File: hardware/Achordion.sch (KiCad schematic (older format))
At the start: 98 parts, among them J1 Power, J10 Jack, J11 Jack, J4 Jack, J5 Jack, J6 Jack, J7 Jack, J8 Jack, J9 Jack, SW2 Button, U4 LM4040C10, U6 TL072, U7 MCP6002, U8 MCP6002, U9 MCP6002

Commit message: Convert PCB to two stacked layers
This completely reworked layout should be much easier to solder and also
follows new front panel layout.

Signed-off-by: Petr Horacek <hrck@protonmail.com>
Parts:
- removed C39: 100n, Capacitor_SMD:C_0603_1608Metric_Pad1.08x0.95mm_HandSolder, symbol Device:C_Small
- removed C45, C47: 3n3, Capacitor_SMD:C_0603_1608Metric_Pad1.08x0.95mm_HandSolder, symbol Device:C_Small
- removed J11: Jack, Connector_Audio:Jack_3.5mm_QingPu_WQP-PJ398SM_Vertical_CircularHoles, symbol Connector:AudioJack2_SwitchT
- removed R15, R16, R49: 10k, Resistor_SMD:R_0603_1608Metric_Pad0.98x0.95mm_HandSolder, symbol Device:R_Small
- removed R32: 200k, Resistor_SMD:R_0603_1608Metric_Pad0.98x0.95mm_HandSolder, symbol Device:R_Small
- removed R33: 100k, Resistor_SMD:R_0603_1608Metric_Pad0.98x0.95mm_HandSolder, symbol Device:R_Small
- removed R34: 33k, Resistor_SMD:R_0603_1608Metric_Pad0.98x0.95mm_HandSolder, symbol Device:R_Small
- removed U7, U8: MCP6002, Package_SO:SOIC-8_3.9x4.9mm_P1.27mm, symbol Amplifier_Operational:MCP6002-xSN
- added J11: A I/O, Connector_PinHeader_2.54mm:PinHeader_2x06_P2.54mm_Vertical, symbol Connector_Generic:Conn_02x06_Odd_Even
- added J12: Debug, Connector_PinHeader_2.54mm:PinHeader_1x05_P2.54mm_Vertical, symbol Connector_Generic:Conn_01x05
- added J13: A IFACE, Connector_PinHeader_2.54mm:PinHeader_2x08_P2.54mm_Vertical, symbol Connector_Generic:Conn_02x08_Odd_Even
- added J2: B IFACE, Connector_PinSocket_2.54mm:PinSocket_2x08_P2.54mm_Vertical, symbol Connector_Generic:Conn_02x08_Odd_Even
- added J3: B I/O, Connector_PinSocket_2.54mm:PinSocket_2x06_P2.54mm_Vertical, symbol Connector_Generic:Conn_02x06_Odd_Even
- added U1: MCP6004, Package_SO:SOIC-14_3.9x8.7mm_P1.27mm, symbol Amplifier_Operational:MCP6004
- A1: value DaisySeed_Rev4 -> Daisy Seed v4; footprint Socket_DaisySeed:DaisySeed -> Device_Audio_Electrosmith_Daisy_Seed:Device_Audio_Electrosmith_Daisy_Seed
- C21: footprint Capacitor_SMD:C_1206_3216Metric_Pad1.33x1.80mm_HandSolder -> Capacitor_SMD:C_0603_1608Metric_Pad1.08x0.95mm_HandSolder
- D10, D3, D4, D5, D6, D7, D8, D9: value LED_Small -> LED
- FB1, FB2: value Ferrite_Bead_Small -> FB
- J1: footprint Connector_PinHeader_2.54mm:PinHeader_2x05_P2.54mm_Vertical -> Connector_IDC:IDC-Header_2x05_P2.54mm_Vertical
- RV1, RV2, RV3, RV4: footprint Potentiometer_THT:Potentiometer_Alps_RK09L_Single_Vertical -> Potentiometer_THT:Potentiometer_Alpha_RD901F-40-00D_Single_Vertical
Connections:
- net +3.3VA: now also J13.7 (Pin_7), J2.7 (Pin_7), U1.4 (V+)
- net CV1: now also A1.24 (ADC_INP5), C41.1, R22.2, U1.7; no longer A1.27 (ADC_INP11), C40.1, R19.2
- net CV2: now also A1.23 (ADC_INP15), C40.1, R19.2, U1.1; no longer A1.26 (ADC_INP3), C41.1, R22.2
- net CV3: now also A1.26 (ADC_INP3), C43.1, R29.2, U1.14; no longer A1.22 (ADC_INP10), C44.1, R31.2, U9.1
- net CV4: now also A1.25 (ADC_INP7), C42.1, R26.2, U1.8; no longer A1.23 (ADC_INP15), U9.7
- net CV5: now also A1.22 (ADC_INP10), C44.1, R31.2, U9.1; no longer A1.24 (ADC_INP5), C42.1, R26.2
- net GND: now also J11.1 (Pin_1), J11.3 (Pin_3), J12.1 (Pin_1), J13.1 (Pin_1), J13.3 (Pin_3), J2.1 (Pin_1), J2.3 (Pin_3), J3.1 (Pin_1), J3.3 (Pin_3), U1.10 (+), U1.11 (V-), U1.12 (+), U1.3 (+), U1.5 (+); no longer U9.5 (+)
- net B_LED8: now reaches A1.1 (USB_HS_ID)
- net B_LED8: now also J2.2 (Pin_2)
- net B_LED7: now reaches A1.2 (SDMMC1_D3)
- net B_LED7: now also J2.4 (Pin_4)
- net B_LED6: now reaches A1.3 (SDMMC1_D2)
- net B_LED6: now also J2.6 (Pin_6)
- net GPIO1: now reaches A1.34 (SAI2_FS_B)
- net GPIO1: now also J12.2 (Pin_2)
- net GPIO2: now reaches A1.35 (SAI2_SCK_B)
- net GPIO2: now also J12.3 (Pin_3)
- net B_LED1: now reaches A1.8 (SPI1_NSS)
- net B_LED1: now also J2.16 (Pin_16)
- net B_BUTTON: now reaches A1.9 (SPI1_SCK)
- net B_BUTTON: now also J2.15 (Pin_15)
- net at J1.1 (Pin_1), J1.2 (Pin_2): now also FB2.2; no longer FB1.2
- net at J1.10 (Pin_10), J1.9 (Pin_9): now also FB1.2; no longer FB2.2
- net A_CV5_IN: now reaches J10.T
- net A_CV5_IN: now also J11.12 (Pin_12); no longer R30.1
- net A_CV3_IN: now reaches J8.T
- net A_CV3_IN: now also J11.8 (Pin_8); no longer R25.1
- net A_CV4_IN: now reaches J9.T
- net A_CV4_IN: now also J11.10 (Pin_10); no longer R28.1
- net A_CV2_IN: now reaches J7.T
- net A_CV2_IN: now also J11.6 (Pin_6); no longer R21.1
- net A_CV1_IN: now reaches J6.T
- net A_CV1_IN: now also J11.4 (Pin_4); no longer R18.1
- net B_OUT1_MAIN: now reaches C36.1, R9.2, U6.1
- net B_OUT1_MAIN: now also J3.11 (Pin_11); no longer R10.1
- net B_OUT2_FALL: now reaches C36.2, R8.2, R9.1, U6.2 (-)
- net B_OUT2_FALL: now also J3.5 (Pin_5); no longer R50.2
- net B_OUT1_FALL: now reaches C38.2, R12.2, R13.1, U6.6 (-)
- net B_OUT1_FALL: now also J3.9 (Pin_9); no longer R51.2
- net B_OUT2_MAIN: now reaches C38.1, R13.2, U6.7
- net B_OUT2_MAIN: now also J3.7 (Pin_7); no longer R14.1
- net A_BUTTON: now reaches SW2.1
- net A_BUTTON: now also J13.15 (Pin_15)
- net at C40.2, R17.2, R18.2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: now also U1.2 (-)
- net at C41.2, R20.2, R21.2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: now also U1.6 (-)
- net at C42.2, R24.2, R25.2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: now also U1.9 (-)
- net at C43.2, R27.2, R28.2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: now also U1.13 (-)
- net BUTTON: no longer names the net of A1.10 (SPI1_MISO)
- removed net CV6: A1.25 (ADC_INP7), C43.1, R29.2
- net LED1 renamed A_LED1
- net A_LED1: now also J13.16 (Pin_16); no longer A1.37 (USB_HS_D_+)
- net LED2 renamed A_LED2
- net A_LED2: now also J13.14 (Pin_14); no longer A1.36 (USB_HS_D_-)
- net LED3: no longer names the net of A1.33 (SAI2_SD_A)
- net LED3: no longer R37.1
- net LED4: no longer names the net of A1.32 (SAI2_SD_B)
- net LED4: no longer R38.1
- net LED5 renamed A_LED5
- net A_LED5: now also J13.8 (Pin_8); no longer A1.4 (SDMMC1_D1)
- net LED6 renamed A_LED6
- net A_LED6: now also J13.6 (Pin_6); no longer A1.5 (SDMMC1_D0)
- net LED7 renamed A_LED7
- net A_LED7: now also J13.4 (Pin_4); no longer A1.6 (SDMMC1_CMD)
- net LED8 renamed A_LED8
- net A_LED8: now also J13.2 (Pin_2); no longer A1.7 (SDMMC1_CK)
- net POT1 renamed A_POT1
- net A_POT1: now also J13.5 (Pin_5); no longer A1.30 (DAC1_OUT1)
- net POT2: no longer names the net of A1.31 (SAI2_MCLK_B)
- net POT2: no longer RV2.2
- net POT3 renamed A_POT3
- net A_POT3: now also J13.13 (Pin_13); no longer A1.29 (DAC1_OUT2)
- net POT4 renamed A_POT4
- net A_POT4: now also J13.11 (Pin_11); no longer A1.28 (ADC1_INP4)
- net PROBE renamed A_PROBE
- net A_PROBE: now also J11.2 (Pin_2); no longer A1.11 (SPI1_MOSI), D11.3
- new net A_LED3: J13.12 (Pin_12), R37.1
- new net A_LED4: J13.10 (Pin_10), R38.1
- new net A_OUT1_FALL: J11.9 (Pin_9), R51.2
- new net A_OUT1_MAIN: J11.11 (Pin_11), R10.1
- new net A_OUT2_FALL: J11.5 (Pin_5), R50.2
- new net A_OUT2_MAIN: J11.7 (Pin_7), R14.1
- new net A_POT2: J13.9 (Pin_9), RV2.2
- new net B_CV1_IN: J3.4 (Pin_4), R21.1
- new net B_CV2_IN: J3.6 (Pin_6), R18.1
- new net B_CV3_IN: J3.8 (Pin_8), R28.1
- new net B_CV4_IN: J3.10 (Pin_10), R25.1
- new net B_CV5_IN: J3.12 (Pin_12), R30.1
- new net B_LED2: A1.7 (SDMMC1_CK), J2.14 (Pin_14)
- new net B_LED3: A1.6 (SDMMC1_CMD), J2.12 (Pin_12)
- new net B_LED4: A1.5 (SDMMC1_D0), J2.10 (Pin_10)
- new net B_LED5: A1.4 (SDMMC1_D1), J2.8 (Pin_8)
- new net B_POT1: A1.27 (ADC_INP11), J2.5 (Pin_5)
- new net B_POT2: A1.28 (ADC1_INP4), J2.9 (Pin_9)
- new net B_POT3: A1.30 (DAC1_OUT1), J2.13 (Pin_13)
- new net B_POT4: A1.29 (DAC1_OUT2), J2.11 (Pin_11)
- new net B_PROBE: A1.11 (SPI1_MOSI), D11.3, J3.2 (Pin_2)
- new net GPIO3: A1.36 (USB_HS_D_-), J12.4 (Pin_4)
- new net GPIO4: A1.37 (USB_HS_D_+), J12.5 (Pin_5)
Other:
- moved on the sheet: C33, C34, C35, C36, C37, C38, C40, C41, C42, C43, C44, C46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

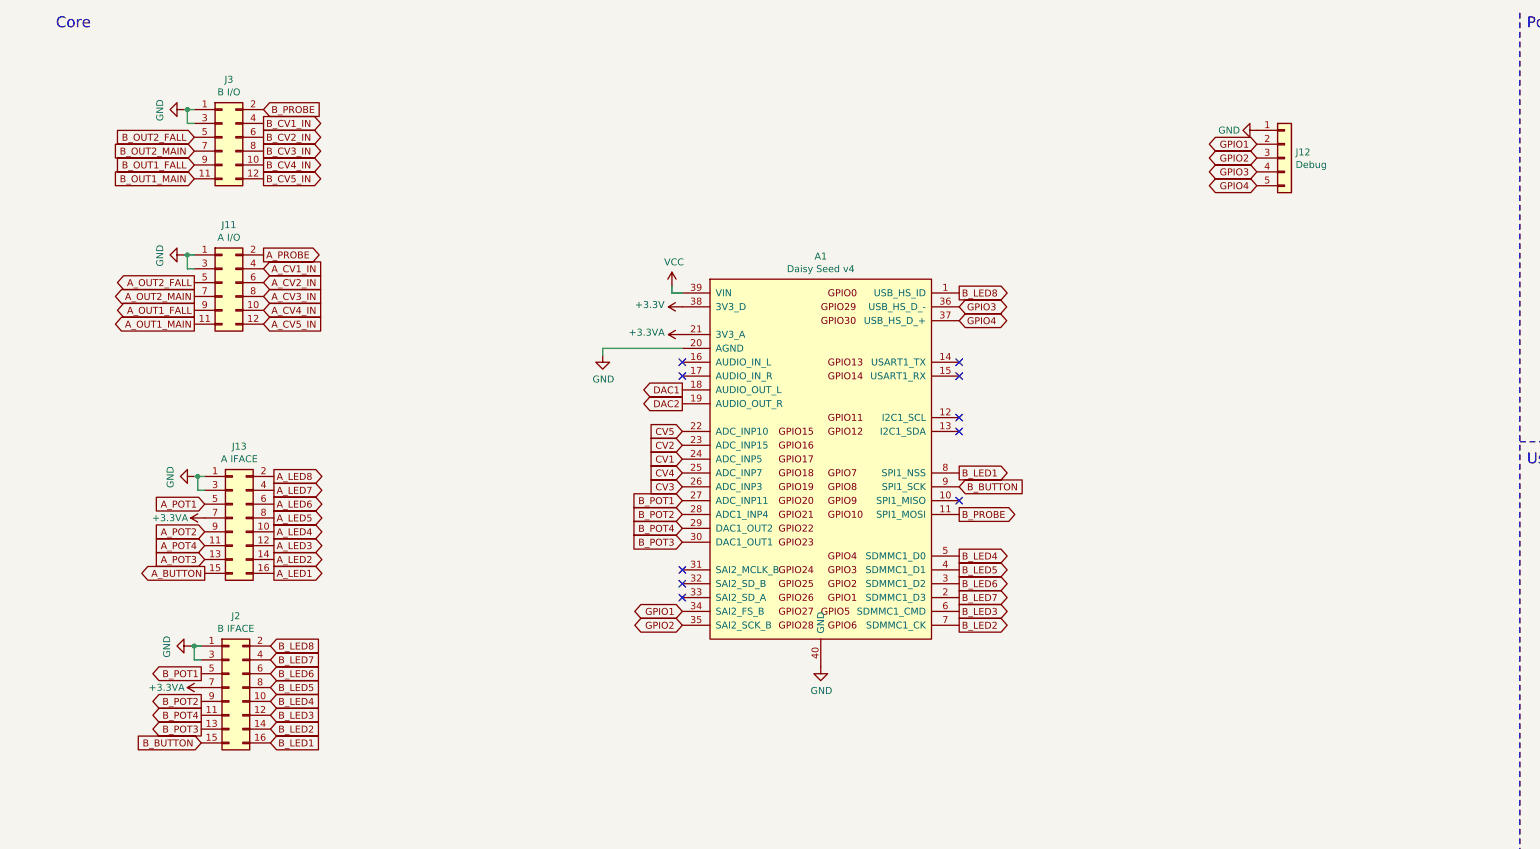
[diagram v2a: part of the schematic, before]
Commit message: Wire compatibility version into the PCB
4 GPIO pins will be signaling version of the hardware to software. This
will allow the software to remain backwards compatible to some degree.

Signed-off-by: Petr Horacek <hrck@protonmail.com>
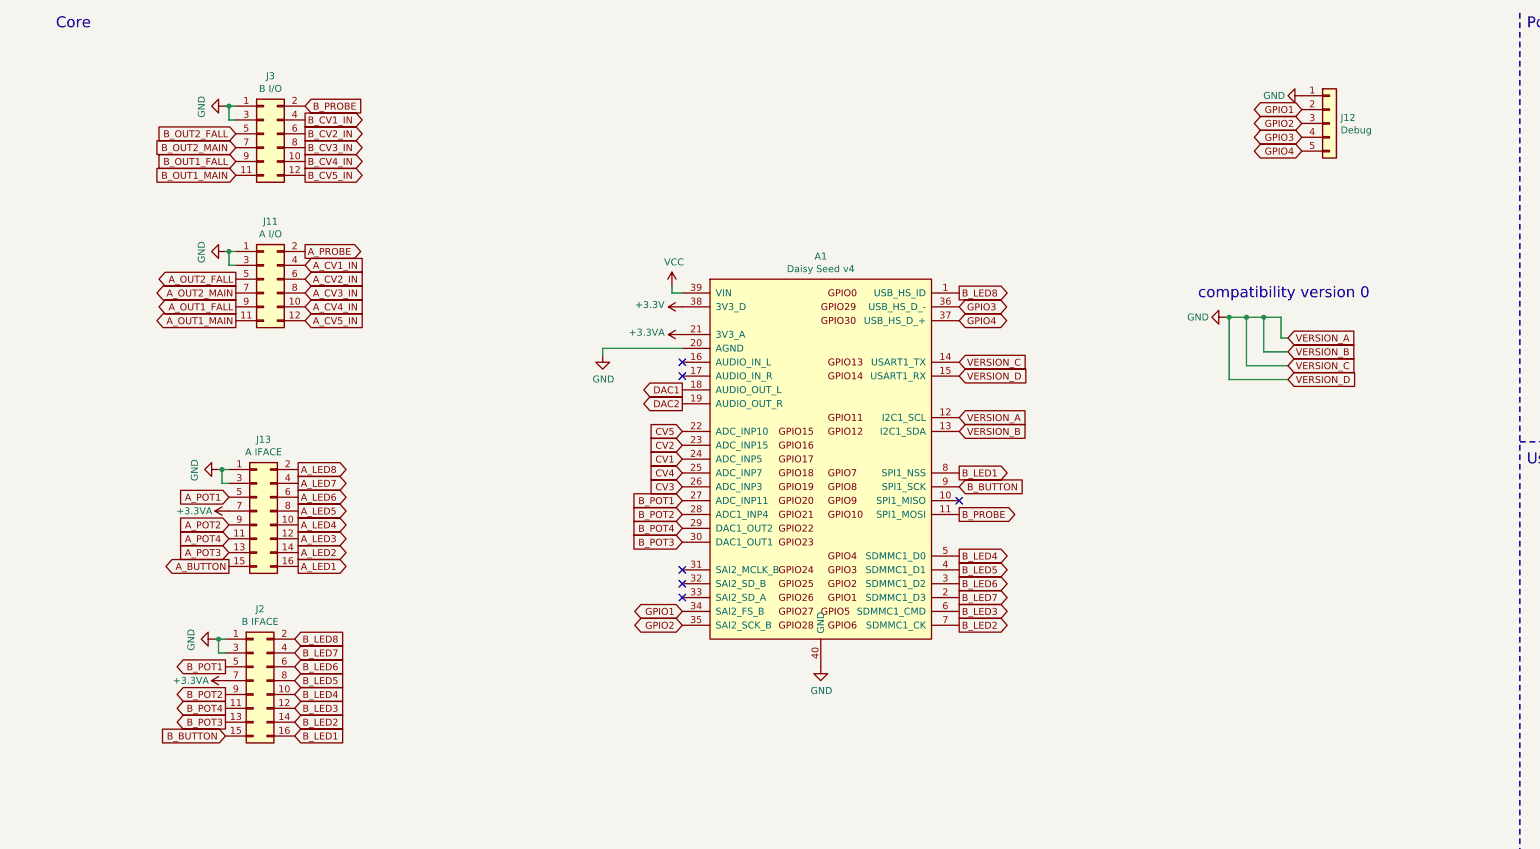
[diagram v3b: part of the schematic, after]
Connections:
- net GND: now also A1.12 (I2C1_SCL), A1.13 (I2C1_SDA), A1.14 (USART1_TX), A1.15 (USART1_RX)
- no-connect marks 13 -> 9
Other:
- note added: "compatibility version 0"
- moved on the sheet: J11, J12, J13, J2, J3

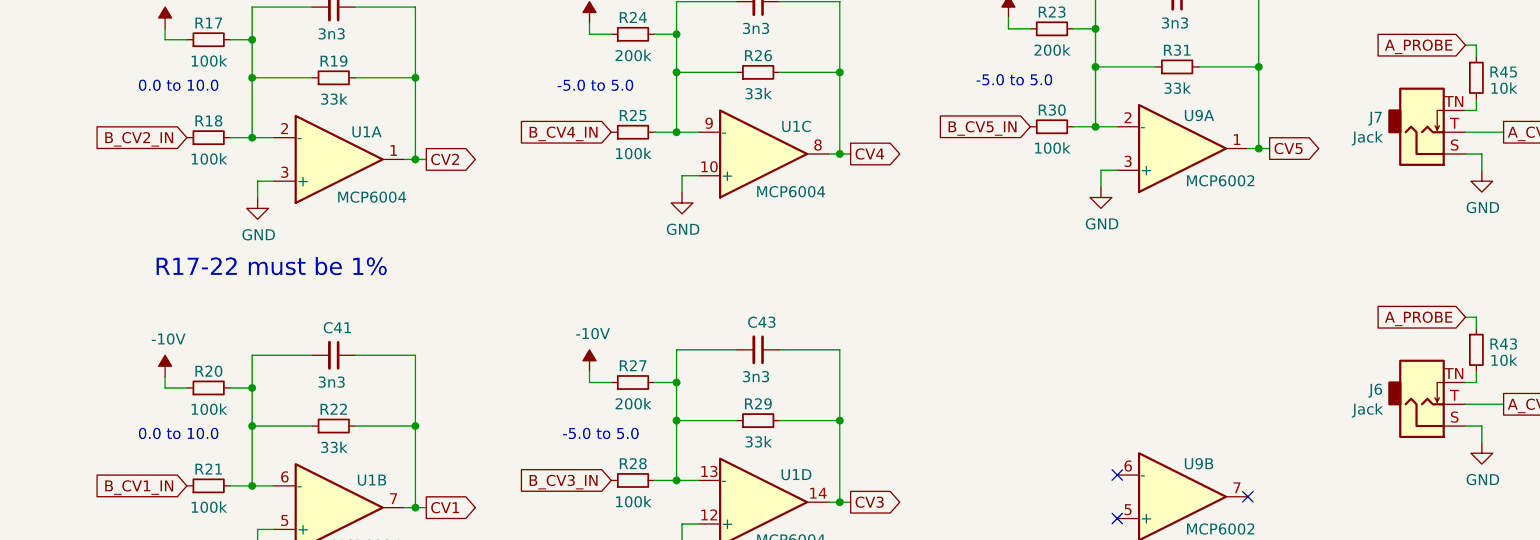
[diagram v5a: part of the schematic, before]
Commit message: State that all CV scaling resistors should be 1%
Signed-off-by: Petr Horacek <hrck@protonmail.com>
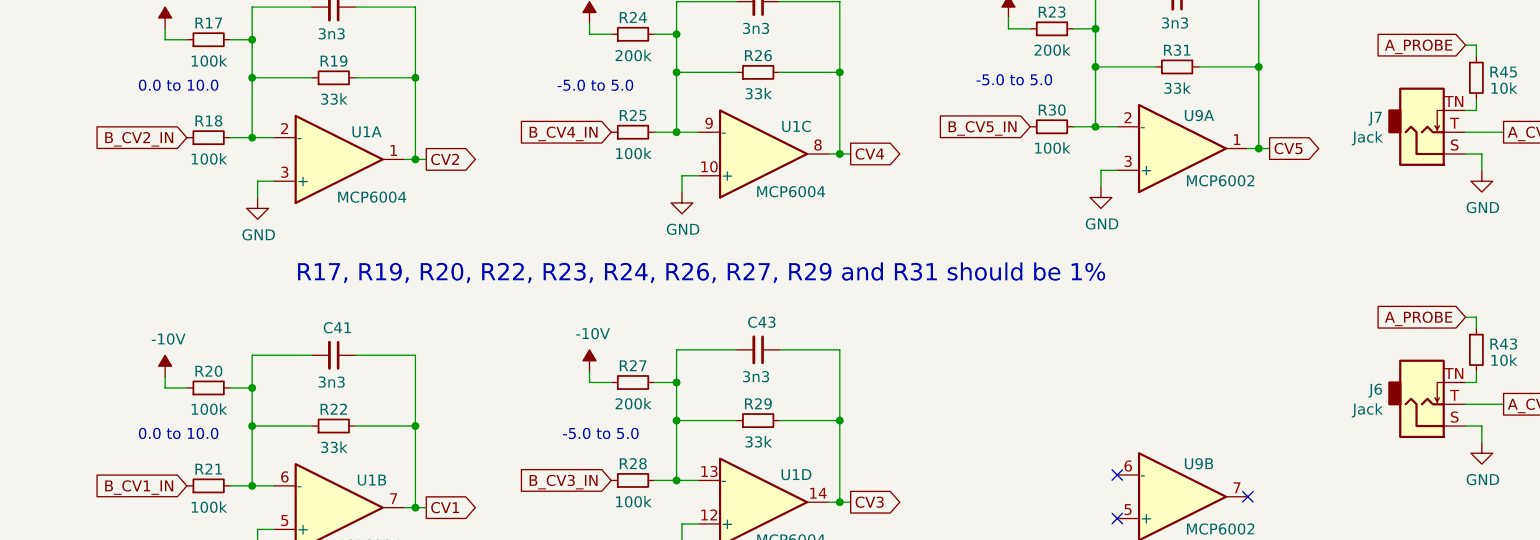
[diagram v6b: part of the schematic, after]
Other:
- note added: "R17, R19, R20, R22, R23, R24, R26, R27, R29 and R31 should be 1%"
- note removed: "R17-22 must be 1%"
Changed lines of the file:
@@
 	0    -1   -1   0
 $EndComp
-Text Notes 1000 8550 0    79   ~ 0
-R17-22 must be 1%
+Text Notes 1650 8575 0    79   ~ 0
+R17, R19, R20, R22, R23, R24, R26, R27, R29 and R31 should be 1%
 $Comp
 L Connector_Generic:Conn_02x08_Odd_Even J13

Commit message: Change the CV range of chord to 0 to 10V
Since chords are a discrete parameter, it makes sense to keep it
quantized in the same way as tone input, suited for keys and sequencers.

Signed-off-by: Petr Horacek <hrck@protonmail.com>
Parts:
- R23: value 200k -> 100k
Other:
- note added: "R17 to R31 should be 1% for best CV accuracy"
- note removed: "R17, R19, R20, R22, R23, R24, R26, R27, R29 and R31 should be 1%"
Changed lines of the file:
@@
 $EndComp
 Text Notes 1650 8575 0    79   ~ 0
-R17, R19, R20, R22, R23, R24, R26, R27, R29 and R31 should be 1%
+R17 to R31 should be 1% for best CV accuracy
 $Comp
 L Connector_Generic:Conn_02x08_Odd_Even J13
@@
 P 5125 7400
 F 0 "R23" V 5200 7400 50  0000 C CNN
-F 1 "200k" V 5025 7400 50  0000 C CNN
+F 1 "100k" V 5025 7400 50  0000 C CNN
 F 2 "Resistor_SMD:R_0603_1608Metric_Pad0.98x0.95mm_HandSolder" H 5125 7400 50  0001 C CNN
 F 3 "~" H 5125 7400 50  0001 C CNN

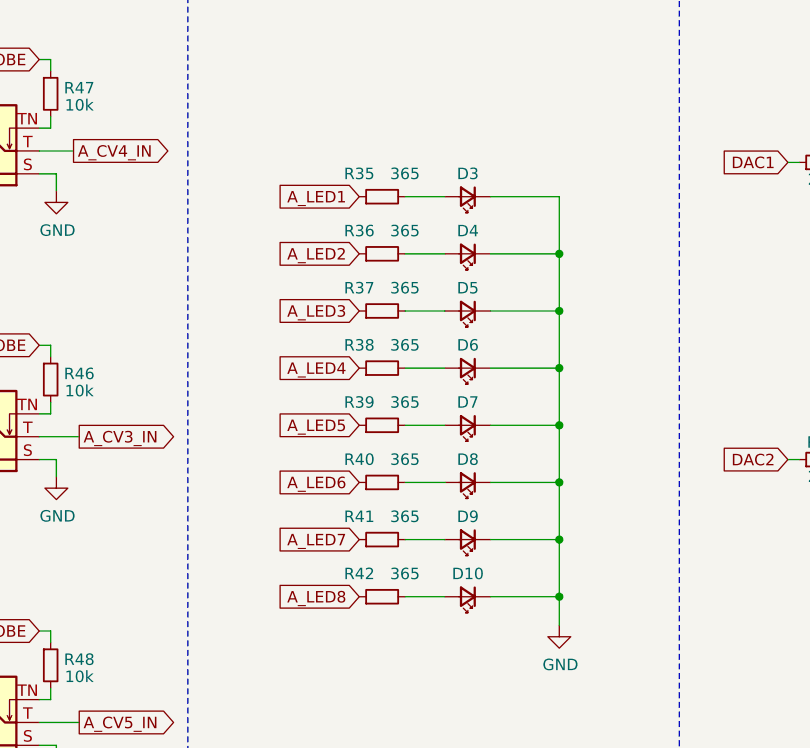
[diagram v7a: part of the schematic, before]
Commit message: Decrease the brightness of LEDs
Replace 365R with 1k. The original was just too bright, especially since
the LEDs serve only as a simple on/off indicator. With the new value,
they should not little less bright but still good enough even on sun.

Signed-off-by: Petr Horacek <hrck@protonmail.com>
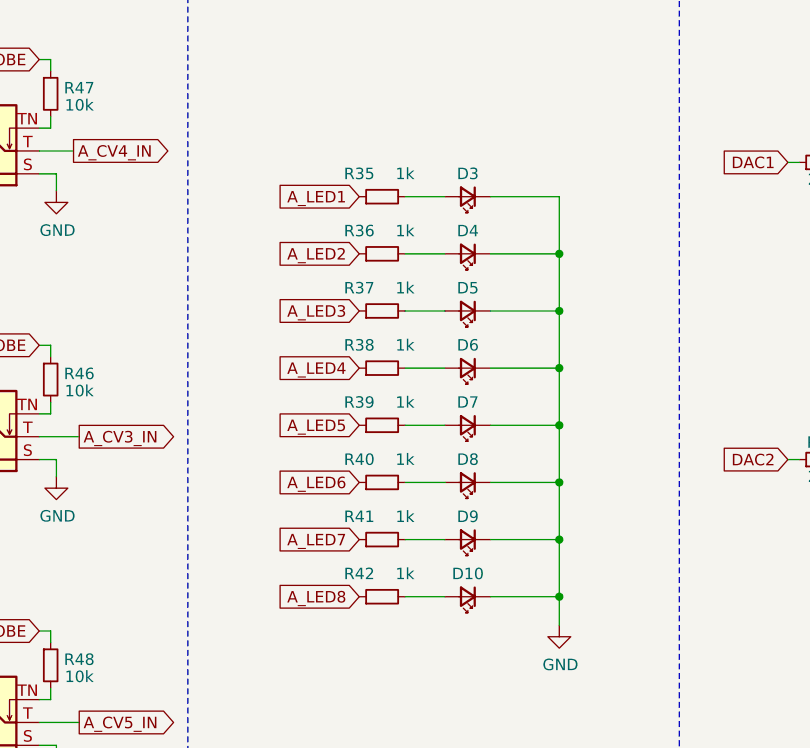
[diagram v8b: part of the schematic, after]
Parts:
- R35, R36, R37, R38, R39, R40, R41, R42: value 365 -> 1k
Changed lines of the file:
@@
 P 9775 9825
 F 0 "R42" V 9875 9925 50  0000 C CNN
-F 1 "365" V 9875 9725 50  0000 C CNN
+F 1 "1k" V 9875 9725 50  0000 C CNN
 F 2 "Resistor_SMD:R_0603_1608Metric_Pad0.98x0.95mm_HandSolder" H 9775 9825 50  0001 C CNN
 F 3 "~" H 9775 9825 50  0001 C CNN
@@
 P 9775 9325
 F 0 "R40" V 9875 9425 50  0000 C CNN
-F 1 "365" V 9875 9225 50  0000 C CNN
+F 1 "1k" V 9875 9225 50  0000 C CNN
 F 2 "Resistor_SMD:R_0603_1608Metric_Pad0.98x0.95mm_HandSolder" H 9775 9325 50  0001 C CNN
 F 3 "~" H 9775 9325 50  0001 C CNN
@@
 P 9775 9075
 F 0 "R39" V 9875 9175 50  0000 C CNN
-F 1 "365" V 9875 8975 50  0000 C CNN
+F 1 "1k" V 9875 8975 50  0000 C CNN
 F 2 "Resistor_SMD:R_0603_1608Metric_Pad0.98x0.95mm_HandSolder" H 9775 9075 50  0001 C CNN
 F 3 "~" H 9775 9075 50  0001 C CNN
@@
 P 9775 8825
 F 0 "R38" V 9875 8925 50  0000 C CNN
-F 1 "365" V 9875 8725 50  0000 C CNN
+F 1 "1k" V 9875 8725 50  0000 C CNN
 F 2 "Resistor_SMD:R_0603_1608Metric_Pad0.98x0.95mm_HandSolder" H 9775 8825 50  0001 C CNN
 F 3 "~" H 9775 8825 50  0001 C CNN
@@
 P 9775 8575
 F 0 "R37" V 9875 8675 50  0000 C CNN
-F 1 "365" V 9875 8475 50  0000 C CNN
+F 1 "1k" V 9875 8475 50  0000 C CNN
 F 2 "Resistor_SMD:R_0603_1608Metric_Pad0.98x0.95mm_HandSolder" H 9775 8575 50  0001 C CNN
 F 3 "~" H 9775 8575 50  0001 C CNN
@@
 P 9775 8325
 F 0 "R36" V 9875 8425 50  0000 C CNN
-F 1 "365" V 9875 8225 50  0000 C CNN
+F 1 "1k" V 9875 8225 50  0000 C CNN
 F 2 "Resistor_SMD:R_0603_1608Metric_Pad0.98x0.95mm_HandSolder" H 9775 8325 50  0001 C CNN
 F 3 "~" H 9775 8325 50  0001 C CNN
@@
 P 9775 8075
 F 0 "R35" V 9875 8175 50  0000 C CNN
-F 1 "365" V 9875 7975 50  0000 C CNN
+F 1 "1k" V 9875 7975 50  0000 C CNN
 F 2 "Resistor_SMD:R_0603_1608Metric_Pad0.98x0.95mm_HandSolder" H 9775 8075 50  0001 C CNN
 F 3 "~" H 9775 8075 50  0001 C CNN
@@
 P 9775 9575
 F 0 "R41" V 9875 9675 50  0000 C CNN
-F 1 "365" V 9875 9475 50  0000 C CNN
+F 1 "1k" V 9875 9475 50  0000 C CNN
 F 2 "Resistor_SMD:R_0603_1608Metric_Pad0.98x0.95mm_HandSolder" H 9775 9575 50  0001 C CNN
 F 3 "~" H 9775 9575 50  0001 C CNN
